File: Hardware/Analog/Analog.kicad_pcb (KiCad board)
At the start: 2 copper layers, 9 parts, among them Q500 IRFZ24NPbF, Q501 IRFZ24NPbF, Q502 IRFZ24NPbF, Q503 IRFZ24NPbF, Q504 IRFZ24NPbF, Q505 IRFZ24NPbF, Q506 IRFZ24NPbF, Q507 IRFZ24NPbF

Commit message: Change one footprint to one that exists
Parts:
- removed Q500, Q501, Q502, Q503, Q504, Q505, Q506, Q507: IRFZ24NPbF, TO-220_plated_mount:TO-220_Horizontal
- moved REF** 623.7 mm to (-440.4, -140.8)
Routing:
- net DUT+: track 250.0 -> 0.00 mm
- net CURRENT_SENSE+: track 30.8 -> 0.00 mm
- removed copper zone on B.Cu, net CURRENT_SENSE+

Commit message: Position load FETs, heatsink mounts, source resistors
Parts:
- added C101: 0.1µF, Capacitors_SMD:C_0603, F.Cu at (186.3, -245.0)
- added C102: 1µF, Capacitors_SMD:C_0603, F.Cu at (190.6, -245.0)
- added C103: 100pF, Capacitors_SMD:C_0603, F.Cu at (206.5, -249.9)
- added C104: 0.1µF, Capacitors_SMD:C_0603, F.Cu at (195.0, -245.0)
- added C105: 150µF, Capacitors_SMD:CP_Elec_6.3x7.7, F.Cu at (-61.3, 86.8)
- added C106: 150µF, Capacitors_SMD:CP_Elec_6.3x7.7, F.Cu at (-71.0, 86.8)
- added C107: 10µF, Capacitors_SMD:C_1206, F.Cu at (527.5, -232.9)
- added C108: 10µF, Capacitors_SMD:C_1206, F.Cu at (522.9, -227.1)
- added C109: 10µF, Capacitors_SMD:C_1206, F.Cu at (218.5, -273.2)
- added C110: 10µF, Capacitors_SMD:C_1206, F.Cu at (223.4, -273.2)
- added C111: 10µF, Capacitors_SMD:C_1206, F.Cu at (218.5, -267.5)
- added C201: 10µF, Capacitors_SMD:C_1206, F.Cu at (80.2, 90.0)
- added C202: 1µF, Capacitors_SMD:C_0603, F.Cu at (76.7, 104.1)
- added C203: 1µF, Capacitors_SMD:C_0603, F.Cu at (85.5, 100.5)
- added C204: 1µF, Capacitors_SMD:C_0603, F.Cu at (85.5, 105.4)
- added C205: 1µF, Capacitors_SMD:C_0603, F.Cu at (65.7, 153.3)
- added C206: 0.1µF, Capacitors_SMD:C_0603, F.Cu at (50.5, 150.4)
- added C207: 1µF, Capacitors_SMD:C_0603, F.Cu at (55.2, 153.5)
- added C208: 1µF, Capacitors_SMD:C_0603, B.Cu at (61.6, 144.2)
- added C209: 1µF, Capacitors_SMD:C_0603, F.Cu at (67.1, 153.3)
- added C210: 0.1µF, Capacitors_SMD:C_0603, F.Cu at (70.1, 116.2)
- added C211: 0.1µF, Capacitors_SMD:C_0603, F.Cu at (81.1, 105.4)
- added C212: 0.1µF, Capacitors_SMD:C_0603, F.Cu at (79.4, 110.4)
- added C213: 0.1µF, Capacitors_SMD:C_0603, B.Cu at (-12.2, 135.6)
- added C214: 0.1µF, Capacitors_SMD:C_0603, F.Cu at (-16.8, 135.4)
- added C215: 0.1µF, Capacitors_SMD:C_0603, F.Cu at (81.1, 100.5)
- added C216: 0.1µF, Capacitors_SMD:C_0603, F.Cu at (93.2, 89.8)
- added C217: 0.1µF, Capacitors_SMD:C_0603, F.Cu at (89.1, 95.1)
- added D101: APG1608ZGCK, LEDs:LED_0603, F.Cu at (54.7, 78.2)
- added D102: APG1608ZGCK, LEDs:LED_0603, F.Cu at (43.8, 78.2)
- added D201: BAT46WQ-7-F, Diodes_SMD:D_SOD-123, F.Cu at (64.3, 90.3)
- added D202: BAT46WQ-7-F, Diodes_SMD:D_SOD-123, F.Cu at (117.2, 136.0)
- added D203: BAT46WQ-7-F, Diodes_SMD:D_SOD-123, F.Cu at (117.2, 146.0)
- added F101: 16V 1.1A 1812, Resistors_SMD:R_1812, F.Cu at (32.5, 79.7)
- added J101: Pomona 4mm 30A connector, Connectors:Banana_Jack_2Pin, F.Cu at (178.3, 205.7)
- added J102: 02x15 IDC, Conn_IDC:IDC-Header_2x15_P2.54mm_Vertical, F.Cu at (120.7, -182.9)
- added M101: MOUNTING_HOLE, Mounting_Holes:MountingHole_3.2mm_M3_Pad, F.Cu at (-59.2, 52.9)
- added M102: MOUNTING_HOLE, Mounting_Holes:MountingHole_3.2mm_M3_Pad, F.Cu at (-71.7, 52.9)
- added M103: MOUNTING_HOLE, Mounting_Holes:MountingHole_3.2mm_M3_Pad, F.Cu at (-71.7, 42.6)
- added M104: MOUNTING_HOLE, Mounting_Holes:MountingHole_3.2mm_M3_Pad, F.Cu at (-59.2, 42.6)
- added Q101: PHP23NQ11T, NikLoad:TO-220_Horizontal, F.Cu at (316.2, -258.3)
- added Q102: PHP23NQ11T, NikLoad:TO-220_Horizontal, F.Cu at (316.2, -247.5)
- added Q103: PHP23NQ11T, NikLoad:TO-220_Horizontal, F.Cu at (316.2, -236.7)
- added Q104: PHP23NQ11T, NikLoad:TO-220_Horizontal, F.Cu at (327.6, -263.3)
- added Q105: PHP23NQ11T, NikLoad:TO-220_Horizontal, F.Cu at (327.6, -252.3)
- added Q106: PHP23NQ11T, NikLoad:TO-220_Horizontal, F.Cu at (327.6, -241.3)
- added Q107: PHP23NQ11T, NikLoad:TO-220_Horizontal, F.Cu at (316.2, -340.4)
- added Q108: PHP23NQ11T, NikLoad:TO-220_Horizontal, F.Cu at (316.2, -329.6)
- added Q109: PHP23NQ11T, NikLoad:TO-220_Horizontal, F.Cu at (316.2, -318.8)
- added Q110: PHP23NQ11T, NikLoad:TO-220_Horizontal, F.Cu at (327.6, -345.4)
- added Q111: PHP23NQ11T, NikLoad:TO-220_Horizontal, F.Cu at (327.6, -334.4)
- added Q112: PHP23NQ11T, NikLoad:TO-220_Horizontal, F.Cu at (327.6, -323.4)
- added Q113: 2N7002, TO_SOT_Packages_SMD:SOT-23, F.Cu at (123.2, 75.9)
- added Q114: 2N7002, TO_SOT_Packages_SMD:SOT-23, F.Cu at (69.3, 79.5)
- added R101: 1k, Resistors_SMD:R_1206, F.Cu at (121.9, -230.6)
- added R102: 100, Resistors_SMD:R_0603, F.Cu at (190.2, -240.1)
- added R103: 100, Resistors_SMD:R_0603, F.Cu at (199.4, -240.1)
- added R104: 100, Resistors_SMD:R_0603, F.Cu at (199.4, -245.0)
- added R105: 100, Resistors_SMD:R_0603, F.Cu at (186.0, -240.1)
- added R106: 100, Resistors_SMD:R_0603, F.Cu at (191.8, -230.3)
- added R107: 100, Resistors_SMD:R_0603, F.Cu at (194.4, -235.2)
- added R108: 100, Resistors_SMD:R_0603, F.Cu at (203.5, -245.0)
- added R109: 100, Resistors_SMD:R_0603, F.Cu at (211.0, -249.9)
- added R110: 100, Resistors_SMD:R_0603, F.Cu at (186.0, -235.2)
- added R111: 100, Resistors_SMD:R_0603, F.Cu at (218.2, -257.2)
- added R112: 100, Resistors_SMD:R_0603, F.Cu at (227.9, -273.5)
- added R113: 100, Resistors_SMD:R_0603, F.Cu at (218.2, -262.1)
- added R114: 100k, Resistors_SMD:R_0603, F.Cu at (54.5, -90.0)
- added R115: 33, Resistors_SMD:R_0603, F.Cu at (58.7, -94.9)
- added R116: 0R02, Resistors_SMD:R_1206, F.Cu at (319.6, -263.3)
- added R117: 0R02, Resistors_SMD:R_1206, F.Cu at (319.6, -252.5)
- added R118: 0R02, Resistors_SMD:R_1206, F.Cu at (319.6, -241.8)
- added R119: 0R02, Resistors_SMD:R_1206, F.Cu at (324.2, -258.2)
- added R120: 0R02, Resistors_SMD:R_1206, F.Cu at (324.2, -247.2)
- added R121: 0R02, Resistors_SMD:R_1206, F.Cu at (324.2, -236.3)
- added R122: 0R02, Resistors_SMD:R_1206, F.Cu at (319.6, -345.4)
- added R123: 0R02, Resistors_SMD:R_1206, F.Cu at (319.6, -334.6)
- added R124: 0R02, Resistors_SMD:R_1206, F.Cu at (319.6, -323.9)
- added R125: 0R02, Resistors_SMD:R_1206, F.Cu at (324.2, -340.3)
- added R126: 0R02, Resistors_SMD:R_1206, F.Cu at (324.2, -329.3)
- added R127: 0R02, Resistors_SMD:R_1206, F.Cu at (324.2, -318.4)
- added R128: 33, Resistors_SMD:R_0603, F.Cu at (54.5, -94.9)
- added R129: 33, Resistors_SMD:R_0603, F.Cu at (62.9, -99.7)
- added R130: 33, Resistors_SMD:R_0603, F.Cu at (187.7, -230.3)
- added R131: 33, Resistors_SMD:R_0603, F.Cu at (62.9, -104.6)
- added R132: 33, Resistors_SMD:R_0603, F.Cu at (58.7, -99.8)
- added R133: 33, Resistors_SMD:R_0603, F.Cu at (58.7, -104.7)
- added R134: 33, Resistors_SMD:R_0603, F.Cu at (54.5, -104.6)
- added R135: 33, Resistors_SMD:R_0603, F.Cu at (190.2, -235.2)
- added R136: 51k1, Resistors_SMD:R_0603, F.Cu at (228.1, -268.6)
- added R137: 51k1, Resistors_SMD:R_0603, F.Cu at (62.9, -94.8)
- added R138: 51k1, Resistors_SMD:R_0603, F.Cu at (54.5, -85.1)
- added R139: 51k1, Resistors_SMD:R_0603, F.Cu at (58.7, -90.0)
- added R140: 51k1, Resistors_SMD:R_0603, F.Cu at (203.5, -240.1)
- added R141: 51k1, Resistors_SMD:R_0603, F.Cu at (228.1, -263.7)
- added R142: 51k1, Resistors_SMD:R_0603, F.Cu at (232.2, -269.2)
- added R143: 51k1, Resistors_SMD:R_0603, F.Cu at (222.4, -258.0)
- added R144: 33, Resistors_SMD:R_0603, F.Cu at (527.4, -227.5)
- added R145: 33, Resistors_SMD:R_0603, F.Cu at (187.7, -225.4)
- added R146: 100, Resistors_SMD:R_0603, F.Cu at (207.7, -245.0)
- added R147: 100, Resistors_SMD:R_0603, F.Cu at (194.4, -240.1)
- added R201: 51k1, Resistors_SMD:R_0603, F.Cu at (70.3, 121.1)
- added R202: 51k1, Resistors_SMD:R_0603, F.Cu at (78.6, 115.3)
- added R203: 20k, Resistors_SMD:R_0805, F.Cu at (110.7, 135.8)
- added R204: 51k1, Resistors_SMD:R_0603, F.Cu at (74.4, 123.8)
- added R205: 51k1, Resistors_SMD:R_0603, F.Cu at (82.8, 115.3)
- added R206: 20k, Resistors_SMD:R_0805, F.Cu at (115.0, 136.8)
- added R207: 20k, Resistors_SMD:R_0805, F.Cu at (53.2, 115.0)
- added R208: 990k, Resistors_SMD:R_1206, F.Cu at (61.8, 105.1)
- added R209: 20k, Resistors_SMD:R_0805, F.Cu at (57.4, 122.5)
- added R210: 1k, Resistors_SMD:R_1206, F.Cu at (116.5, 139.7)
- added R211: 2mOhm, NikLoad:R_3920, F.Cu at (123.0, 141.0)
- added R212: 41.2k, Resistors_SMD:R_1206, F.Cu at (44.7, 121.0)
- added R213: 1k, Resistors_SMD:R_1206, F.Cu at (116.5, 142.2)
- added R214: 20k, Resistors_SMD:R_0805, F.Cu at (53.2, 120.3)
- added R215: 20k, Resistors_SMD:R_0805, B.Cu at (62.6, 151.0)
- added R216: 20k, Resistors_SMD:R_0805, F.Cu at (110.8, 146.1)
- added R217: 20k, Resistors_SMD:R_0805, F.Cu at (115.0, 145.1)
- added R218: 20k, Resistors_SMD:R_0805, F.Cu at (65.7, 111.4)
- added R219: 20k, Resistors_SMD:R_0805, F.Cu at (68.8, 153.2)
- added R220: 10k, Resistors_SMD:R_0603, F.Cu at (74.4, 118.9)
- added R221: 33, Resistors_SMD:R_0603, F.Cu at (55.3, 152.0)
- added R222: 51k1, Resistors_SMD:R_0603, F.Cu at (93.8, 99.6)
- added R223: 51k1, Resistors_SMD:R_0603, F.Cu at (89.6, 104.9)
- added R224: 51k1, Resistors_SMD:R_0603, F.Cu at (89.6, 100.0)
- added R225: 60k4, Resistors_SMD:R_0603, F.Cu at (92.1, 109.8)
- added R226: 51k1, Resistors_SMD:R_0603, F.Cu at (78.6, 120.2)
- added R227: 51k1, Resistors_SMD:R_0603, F.Cu at (93.8, 104.5)
- added R228: 51k1, Resistors_SMD:R_0603, F.Cu at (87.9, 110.3)
- added R229: 20k, Resistors_SMD:R_0805, F.Cu at (84.7, 95.3)
- added R230: 20k, Resistors_SMD:R_0805, F.Cu at (88.9, 89.9)
- added R231: 20k, Resistors_SMD:R_0805, B.Cu at (45.6, 176.6)
- added R232: 20k, Resistors_SMD:R_0805, B.Cu at (42.8, 176.8)
- added REF**: WATERCOOLER_MOUNT, pc_cooler_mount:PC_COOLER_MOUNT, F.Cu at (321.9, -332.1)
- added RV101: 5V, Resistors_SMD:R_0603, F.Cu at (186.5, -249.9)
- added RV102: 5V, Resistors_SMD:R_0603, F.Cu at (223.5, -267.8)
- added RV103: 5V, Resistors_SMD:R_0603, F.Cu at (191.5, -249.9)
- added RV104: 5V, Resistors_SMD:R_0603, F.Cu at (223.5, -262.9)
- added RV105: 5V, Resistors_SMD:R_0603, F.Cu at (125.1, 69.7)
- added RV106: 5V, Resistors_SMD:R_0603, F.Cu at (186.5, -254.8)
- added RV107: 5V, Resistors_SMD:R_0603, F.Cu at (191.5, -254.8)
- added RV108: 5V, Resistors_SMD:R_0603, F.Cu at (196.5, -254.8)
- added RV109: 5V, Resistors_SMD:R_0603, F.Cu at (201.5, -254.8)
- added RV110: 5V, Resistors_SMD:R_0603, F.Cu at (206.5, -254.8)
- added RV111: 5V, Resistors_SMD:R_0603, F.Cu at (211.5, -254.8)
- added RV112: 5V, Resistors_SMD:R_0603, F.Cu at (196.5, -249.9)
- added RV113: 5V, Resistors_SMD:R_0603, F.Cu at (201.5, -249.9)
- added U101: OPA180, TO_SOT_Packages_SMD:SOT-23-5, F.Cu at (63.2, 79.9)
- added U102: 74HC595, Housings_SOIC:SOIC-16_3.9x9.9mm_Pitch1.27mm, F.Cu at (71.9, 68.5)
- added U103: NCP1117DT50G, TO_SOT_Packages_SMD:TO-252-2, F.Cu at (90.6, 54.4)
- added U104: SPX1117-33, TO_SOT_Packages_SMD:SOT-223-3_TabPin2, F.Cu at (117.6, 67.0)
- added U201: OPA388, Housings_SOIC:SOIC-8_3.9x4.9mm_Pitch1.27mm, F.Cu at (30.6, 119.2)
- added U202: OPA388, Housings_SOIC:SOIC-8_3.9x4.9mm_Pitch1.27mm, F.Cu at (55.6, 98.9)
- added U203: OPA388, Housings_SOIC:SOIC-8_3.9x4.9mm_Pitch1.27mm, F.Cu at (73.9, 91.8)
- added U204: OPA388, Housings_SOIC:SOIC-8_3.9x4.9mm_Pitch1.27mm, F.Cu at (106.2, 140.9)
- added U205: ADS127L01, Housings_QFP:LQFP-32_5x5mm_Pitch0.5mm, F.Cu at (60.9, 150.3)
- added U206: TXETCLSANF-16.384MHz, Crystals:Crystal_SMD_3225-4pin_3.2x2.5mm, F.Cu at (50.9, 152.9)
- added U207: NX3L4357, NikLoad:NX3L4357, F.Cu at (38.4, 120.8)
- added U208: MCP4921T-E/MS, Housings_SSOP:MSOP-8_3x3mm_Pitch0.65mm, F.Cu at (52.0, 90.9)
- added U209: OPA388, Housings_SOIC:SOIC-8_3.9x4.9mm_Pitch1.27mm, F.Cu at (45.5, 176.4)
- added U210: DAC8560, Housings_SSOP:VSSOP-8_3.0x3.0mm_Pitch0.65mm, F.Cu at (-12.2, 136.5)
- added U211: MAX6126AASA25+, Housings_SOIC:SOIC-8_3.9x4.9mm_Pitch1.27mm, F.Cu at (33.5, 98.6)
- moved REF** 770.1 mm to (321.9, -250.0)
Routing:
- net Net-(D203-Pad1): track 0.00 -> 10.6 mm
- net Net-(D202-Pad1): track 0.00 -> 10.5 mm
- net /CurrentSense: track 0.00 -> 9.98 mm
- net Net-(R215-Pad1): track 0.00 -> 7.87 mm, vias 0 -> 1
- net /Measurement/SenseResistor: track 0.00 -> 6.99 mm
- net /Measurement/DUT-: track 0.00 -> 6.98 mm
- net Net-(R231-Pad2): track 0.00 -> 6.39 mm, vias 0 -> 2
- net +3V3: track 0.00 -> 5.68 mm, vias 0 -> 1
- net /Measurement/Vref: track 0.00 -> 5.35 mm, vias 0 -> 1
- net Net-(C209-Pad1): track 0.00 -> 3.71 mm
- net Net-(R203-Pad1): track 0.00 -> 3.35 mm
- net Net-(R216-Pad2): track 0.00 -> 3.25 mm
- net /Setpoint: track 0.00 -> 3.18 mm, vias 0 -> 1
- net Net-(C207-Pad1): track 0.00 -> 3.11 mm
- net Net-(R221-Pad1): track 0.00 -> 2.55 mm
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
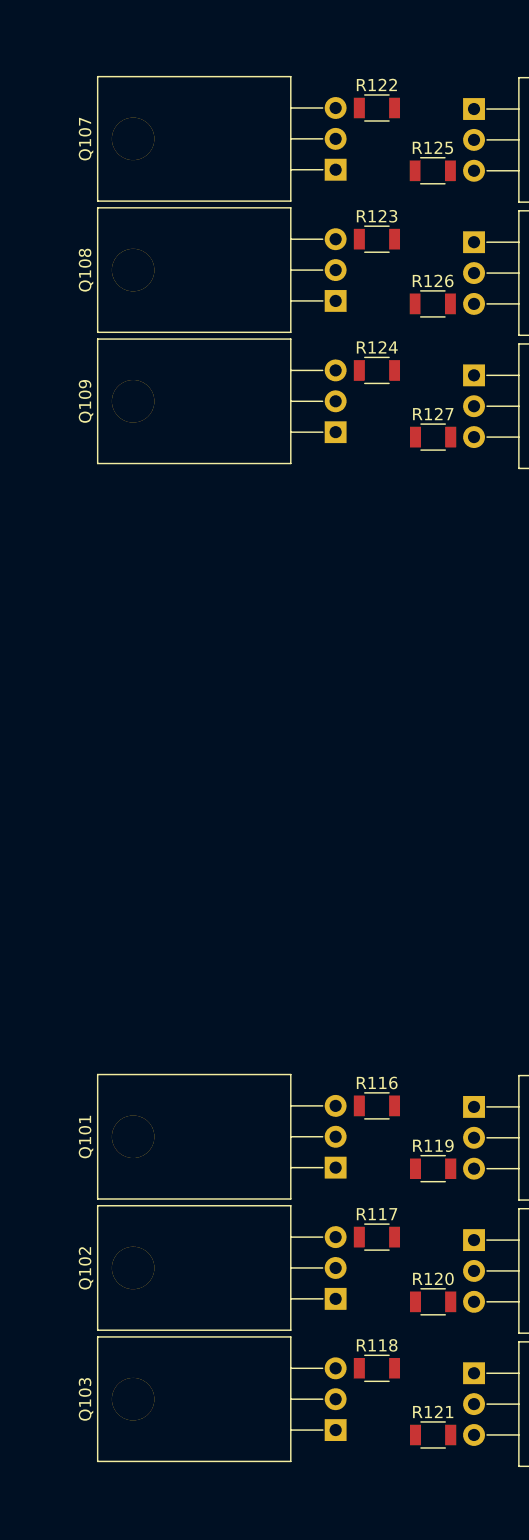
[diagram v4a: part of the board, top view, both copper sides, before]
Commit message: Fix mistake in MOSFET spacing
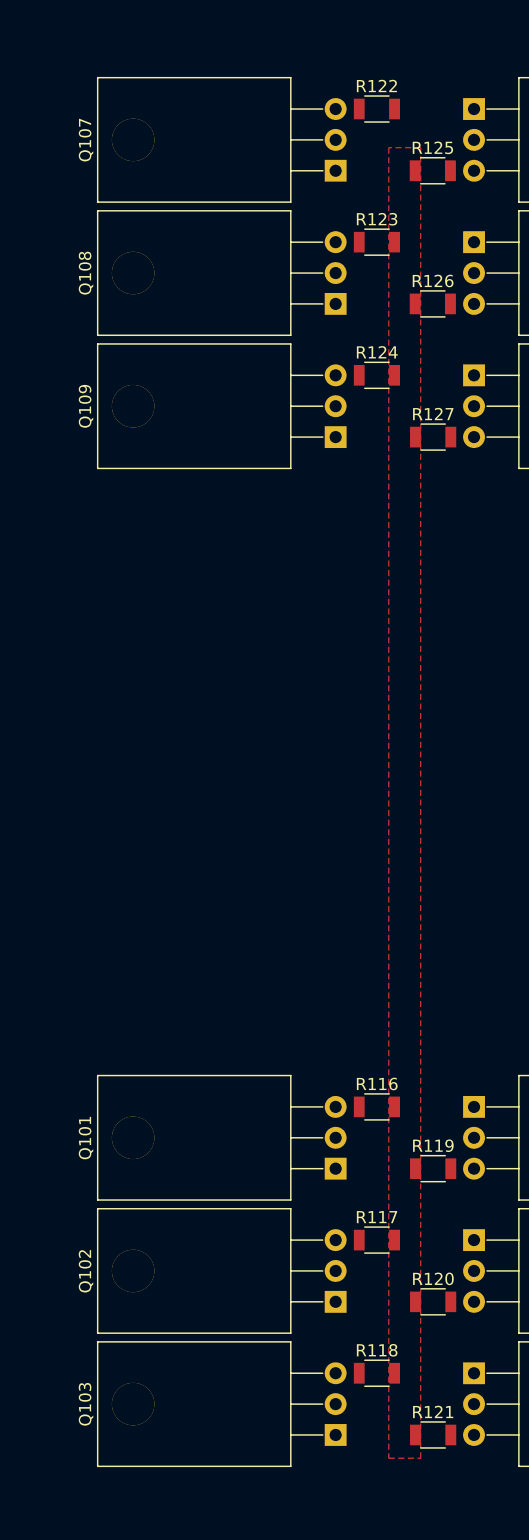
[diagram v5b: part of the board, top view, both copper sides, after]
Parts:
- moved R124 0.41 mm to (319.6, -323.4)
- moved Q103 0.41 mm to (316.2, -236.3)
- moved R118 0.41 mm to (319.6, -241.3)
- moved Q109 0.40 mm to (316.2, -318.4)
- moved Q102 0.25 mm to (316.2, -247.2)
- moved Q108 0.25 mm to (316.2, -329.3)
- moved R123 0.25 mm to (319.6, -334.4)
- moved R117 0.24 mm to (319.6, -252.3)
- moved Q107 0.09 mm to (316.2, -340.3)
- moved Q101 0.08 mm to (316.2, -258.2)
- moved R116 0.08 mm to (319.6, -263.3)
- moved R122 0.08 mm to (319.6, -345.4)
- turned R119 to 180 degrees
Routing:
- added copper zone on F.Cu, net /Measurement/SenseResistor
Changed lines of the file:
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@@
 (kicad_pcb (version 4) (host pcbnew 4.0.7)
   (general
-    (links 0)
-    (no_connects 349)
-    (area -77.9 -371.5274 535.5774 213.0574)
+    (links 353)
+    (no_connects 313)
+    (area -77.9 -371.5274 529.964802 213.0574)
     (thickness 1.6)
     (drawings 0)
@@
   )
   (module NikLoad:TO-220_Horizontal (layer F.Cu)
-    (at 316.23 -258.26 90)
+    (at 316.23 -258.175 90)
     (descr "TO-220, Horizontal, RM 2.54mm")
     (tags "TO-220 Horizontal RM 2.54mm")
@@
   )
   (module NikLoad:TO-220_Horizontal (layer F.Cu)
-    (at 316.23 -247.465 90)
+    (at 316.23 -247.22 90)
     (descr "TO-220, Horizontal, RM 2.54mm")
     (tags "TO-220 Horizontal RM 2.54mm")
@@
   )
   (module NikLoad:TO-220_Horizontal (layer F.Cu)
-    (at 316.23 -236.67 90)
+    (at 316.23 -236.265 90)
     (descr "TO-220, Horizontal, RM 2.54mm")
     (tags "TO-220 Horizontal RM 2.54mm")
@@
   )
   (module NikLoad:TO-220_Horizontal (layer F.Cu)
-    (at 316.23 -340.36 90)
+    (at 316.23 -340.275 90)
     (descr "TO-220, Horizontal, RM 2.54mm")
     (tags "TO-220 Horizontal RM 2.54mm")
@@
   )
   (module NikLoad:TO-220_Horizontal (layer F.Cu)
-    (at 316.23 -329.565 90)
+    (at 316.23 -329.32 90)
     (descr "TO-220, Horizontal, RM 2.54mm")
     (tags "TO-220 Horizontal RM 2.54mm")
@@
   )
   (module NikLoad:TO-220_Horizontal (layer F.Cu)
-    (at 316.23 -318.77 90)
+    (at 316.23 -318.365 90)
     (descr "TO-220, Horizontal, RM 2.54mm")
     (tags "TO-220 Horizontal RM 2.54mm")
@@
   )
   (module Resistors_SMD:R_1206 (layer F.Cu)
-    (at 319.625 -263.34)
+    (at 319.625 -263.255)
     (descr "Resistor SMD 1206, reflow soldering, Vishay (see dcrcw.pdf)")
     (tags "resistor 1206")
@@
   )
   (module Resistors_SMD:R_1206 (layer F.Cu)
-    (at 319.625 -252.545)
+    (at 319.625 -252.3)
     (descr "Resistor SMD 1206, reflow soldering, Vishay (see dcrcw.pdf)")
     (tags "resistor 1206")
@@
   )
   (module Resistors_SMD:R_1206 (layer F.Cu)
-    (at 319.625 -241.75)
+    (at 319.625 -241.345)
     (descr "Resistor SMD 1206, reflow soldering, Vishay (see dcrcw.pdf)")
     (tags "resistor 1206")
@@
   )
   (module Resistors_SMD:R_1206 (layer F.Cu)
-    (at 324.25 -258.175)
+    (at 324.25 -258.175 180)
     (descr "Resistor SMD 1206, reflow soldering, Vishay (see dcrcw.pdf)")
     (tags "resistor 1206")
     (attr smd)
-    (fp_text reference R119 (at 0 -1.85) (layer F.SilkS)
+    (fp_text reference R119 (at 0 1.85 180) (layer F.SilkS)
       (effects (font (size 1 1) (thickness 0.15)))
     )
-    (fp_text value 0R02 (at 0 1.95) (layer F.Fab)
+    (fp_text value 0R02 (at 0 1.95 180) (layer F.Fab)
       (effects (font (size 1 1) (thickness 0.15)))
     )
-    (fp_text user %R (at 0 0) (layer F.Fab)
+    (fp_text user %R (at 0 0 180) (layer F.Fab)
       (effects (font (size 0.7 0.7) (thickness 0.105)))
     )
@@
     (fp_line (start 2.15 1.1) (end 2.15 -1.11) (layer F.CrtYd) (width 0.05))
     (fp_line (start 2.15 1.1) (end -2.15 1.1) (layer F.CrtYd) (width 0.05))
-    (pad 1 smd rect (at -1.45 0) (size 0.9 1.7) (layers F.Cu F.Paste F.Mask)
+    (pad 1 smd rect (at -1.45 0 180) (size 0.9 1.7) (layers F.Cu F.Paste F.Mask)
       (net 44 "Net-(Q104-Pad3)"))
-    (pad 2 smd rect (at 1.45 0) (size 0.9 1.7) (layers F.Cu F.Paste F.Mask)
+    (pad 2 smd rect (at 1.45 0 180) (size 0.9 1.7) (layers F.Cu F.Paste F.Mask)
       (net 65 /Measurement/SenseResistor))
     (model ${KISYS3DMOD}/Resistors_SMD.3dshapes/R_1206.wrl
@@
   )
   (module Resistors_SMD:R_1206 (layer F.Cu)
-    (at 319.625 -345.44)
+    (at 319.625 -345.355)
     (descr "Resistor SMD 1206, reflow soldering, Vishay (see dcrcw.pdf)")
     (tags "resistor 1206")
@@
   )
   (module Resistors_SMD:R_1206 (layer F.Cu)
-    (at 319.625 -334.645)
+    (at 319.625 -334.4)
     (descr "Resistor SMD 1206, reflow soldering, Vishay (see dcrcw.pdf)")
     (tags "resistor 1206")
@@
   )
   (module Resistors_SMD:R_1206 (layer F.Cu)
-    (at 319.625 -323.85)
+    (at 319.625 -323.445)
     (descr "Resistor SMD 1206, reflow soldering, Vishay (see dcrcw.pdf)")
     (tags "resistor 1206")
@@
   (segment (start 44.65 176.55) (end 44.65 175.25) (width 0.1524) (layer B.Cu) (net 108))
   (via (at 44.65 175.25) (size 0.6) (drill 0.3) (layers F.Cu B.Cu) (net 108))
+  (zone (net 65) (net_name /Measurement/SenseResistor) (layer F.Cu) (hatch edge 0.508)
+    (priority 10)
+    (connect_pads (clearance 0.1524))
+    (min_thickness 0.254)
+    (fill yes (arc_segments 16) (thermal_gap 0.2) (thermal_bridge_width 0.6) (smoothing chamfer))
+    (polygon
+      (pts
+        (xy 323.225 -234.35) (xy 323.225 -342.175) (xy 320.6 -342.175) (xy 320.6 -234.35)
+      )
+    )
+  )
 )
